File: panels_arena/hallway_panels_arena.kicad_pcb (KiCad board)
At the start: 2 copper layers, 342.9 x 31.8 mm, 20 parts, among them J1 DB9, J2 DB9, P1 CONN_5X2, P10 CONN_8, P11 CONN_8, P12 CONN_8, P13 CONN_8, P2 CONN_4X2, P3 CONN_2, P4 CONN_5X2, P5 CONN_4X2, P6 CONN_2, P7 CONN_8, P8 CONN_8, P9 CONN_8, SW1 SWITCH_INV

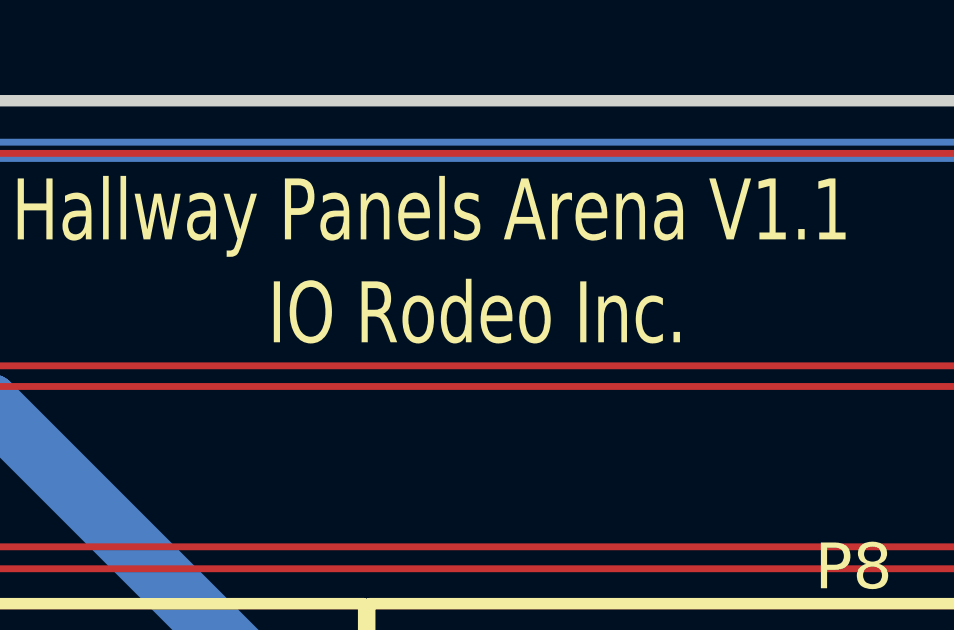
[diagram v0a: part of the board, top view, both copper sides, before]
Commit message: Added a version of PCBs with Dickinson Lab on them instead of IO Rodeo.
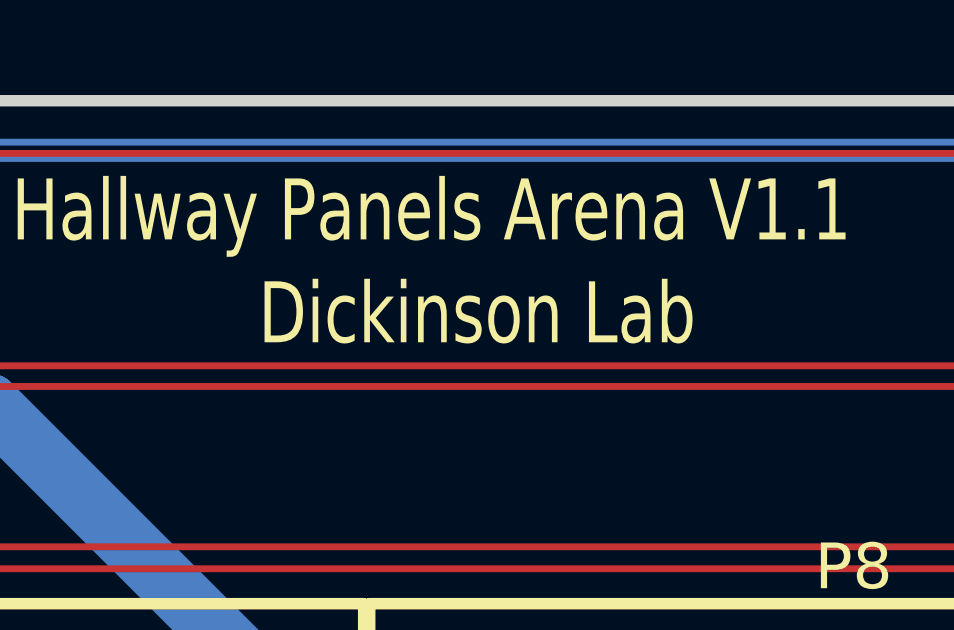
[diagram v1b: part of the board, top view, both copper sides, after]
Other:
- board text added: "Dickinson Lab"
- board text removed: "IO Rodeo Inc."
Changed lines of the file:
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@@
       (drillshape 0)
       (scaleselection 1)
-      (outputdirectory "gerber_v1p1/"))
+      (outputdirectory "gerber_v1p1_dickinson/"))
   )
   (net 0 "")
@@
     (effects (font (size 2.032 1.524) (thickness 0.3048)))
   )
-  (gr_text "IO Rodeo Inc. " (at 125.73 67.437) (layer F.SilkS)
+  (gr_text "Dickinson Lab" (at 125.73 67.437) (layer F.SilkS)
     (effects (font (size 2.032 1.524) (thickness 0.3048)))
   )
